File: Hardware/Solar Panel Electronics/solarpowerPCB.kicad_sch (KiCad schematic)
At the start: 45 parts, among them J3 Conn_01x02_Male, J4 Conn_01x06_Male, J5 Conn_01x02_Male, Q1 MMDT2222A, U1 SN65HVD230, U2 ESP32-PICO-D4

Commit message: Started pcb layout
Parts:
- gave numbers to parts that had none: 4
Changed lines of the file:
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@@
   (symbol (lib_id "Device:L") (at 137.16 26.67 90) (unit 1)
     (in_bom yes) (on_board yes)
-    (property "Reference" "L?" (id 0) (at 137.16 21.844 90))
+    (property "Reference" "L3" (id 0) (at 137.16 21.844 90))
     (property "Value" "LQG15WZ1N8B02D" (id 1) (at 137.16 24.1554 90))
     (property "Footprint" "Inductor_SMD:L_0603_1608Metric_Pad1.05x0.95mm_HandSolder" (id 2) (at 137.16 26.67 0)
@@
   (symbol (lib_id "Device:C_Small") (at 140.97 31.75 0) (unit 1)
     (in_bom yes) (on_board yes)
-    (property "Reference" "C?" (id 0) (at 143.3068 30.5816 0)
+    (property "Reference" "C39" (id 0) (at 143.3068 30.5816 0)
       (effects (font (size 1.27 1.27)) (justify left))
     )
@@
   (symbol (lib_id "Device:C_Small") (at 133.35 31.75 0) (unit 1)
     (in_bom yes) (on_board yes)
-    (property "Reference" "C?" (id 0) (at 128.27 30.48 0)
+    (property "Reference" "C38" (id 0) (at 128.27 30.48 0)
       (effects (font (size 1.27 1.27)) (justify left))
     )
@@
   (symbol (lib_id "iclr:AMCA31-2R450G-S1F-T3") (at 146.05 26.67 270) (unit 1)
     (in_bom yes) (on_board yes)
-    (property "Reference" "ANT?" (id 0) (at 154.7876 25.3746 90)
+    (property "Reference" "ANT1" (id 0) (at 154.7876 25.3746 90)
       (effects (font (size 1.27 1.27)) (justify left))
     )
@@
   (symbol (lib_id "power:GND") (at 133.35 34.29 0) (unit 1)
     (in_bom yes) (on_board yes)
-    (property "Reference" "#PWR?" (id 0) (at 133.35 40.64 0)
+    (property "Reference" "#PWR0136" (id 0) (at 133.35 40.64 0)
       (effects (font (size 1.27 1.27)) hide)
     )
@@
   (symbol (lib_id "power:GND") (at 140.97 34.29 0) (unit 1)
     (in_bom yes) (on_board yes)
-    (property "Reference" "#PWR?" (id 0) (at 140.97 40.64 0)
+    (property "Reference" "#PWR0137" (id 0) (at 140.97 40.64 0)
       (effects (font (size 1.27 1.27)) hide)
     )
@@
       (reference "#PWR0135") (unit 1) (value "+3.3V") (footprint "")
     )
+    (path "/673f1a23-6661-4620-90df-f91c1a23f2f1"
+      (reference "#PWR0136") (unit 1) (value "GND") (footprint "")
+    )
+    (path "/d476ee99-f915-47bb-bc5d-98e60df88272"
+      (reference "#PWR0137") (unit 1) (value "GND") (footprint "")
+    )
+    (path "/bc16b27f-da78-4399-84ff-d0e67df4623d/a8cbb7ea-4783-4a46-908f-66157147a7f8"
+      (reference "#PWR0138") (unit 1) (value "GND") (footprint "")
+    )
     (path "/00000000-0000-0000-0000-0000624b2440/00000000-0000-0000-0000-000062471654"
       (reference "#PWR0145") (unit 1) (value "GND") (footprint "")
@@
       (reference "#PWR0150") (unit 1) (value "GND") (footprint "")
     )
-    (path "/673f1a23-6661-4620-90df-f91c1a23f2f1"
-      (reference "#PWR?") (unit 1) (value "GND") (footprint "")
-    )
-    (path "/d476ee99-f915-47bb-bc5d-98e60df88272"
-      (reference "#PWR?") (unit 1) (value "GND") (footprint "")
-    )
     (path "/661e63a6-57d4-4bd6-8435-e9e47baf2ef9"
-      (reference "ANT?") (unit 1) (value "AMCA31-2R450G-S1F-T3") (footprint "iclr:ANT_AMCA31-2R450G-S1F-T3")
+      (reference "ANT1") (unit 1) (value "AMCA31-2R450G-S1F-T3") (footprint "iclr:ANT_AMCA31-2R450G-S1F-T3")
     )
     (path "/00000000-0000-0000-0000-0000620b2ec1"
@@
       (reference "C37") (unit 1) (value "10uF") (footprint "Capacitor_SMD:C_0603_1608Metric")
     )
+    (path "/58323f1b-ca2a-4c1d-b699-a594d763332c"
+      (reference "C38") (unit 1) (value "33pF") (footprint "Capacitor_SMD:C_0603_1608Metric")
+    )
     (path "/43108d1f-6fab-4012-bb34-effc39df9879"
-      (reference "C?") (unit 1) (value "100pF") (footprint "Capacitor_SMD:C_0603_1608Metric")
-    )
-    (path "/58323f1b-ca2a-4c1d-b699-a594d763332c"
-      (reference "C?") (unit 1) (value "33pF") (footprint "Capacitor_SMD:C_0603_1608Metric")
+      (reference "C39") (unit 1) (value "100pF") (footprint "Capacitor_SMD:C_0603_1608Metric")
     )
     (path "/0b74af2e-d916-4a23-ae3b-0ce9a9c64af1"
@@
     )
     (path "/1cf3aab9-4829-448a-a3c1-5a595217a91d/d4a89851-f343-4a84-b3cb-1339eebcb206"
-      (reference "J7") (unit 1) (value "~") (footprint "Connector_Card:microSD_HC_Hirose_DM3AT-SF-PEJM5")
+      (reference "J7") (unit 1) (value "~") (footprint "Connector_Card:microSD_HC_Wuerth_693072010801")
     )
     (path "/00000000-0000-0000-0000-0000624b2440/357ce087-9bb2-449e-8dc8-378603d15219"
@@
       (reference "J13") (unit 1) (value "Battery Connector") (footprint "Connector_JST:JST_ACH_BM02B-ACHSS-GAN-ETF_1x02-1MP_P1.20mm_Vertical")
     )
+    (path "/bc16b27f-da78-4399-84ff-d0e67df4623d/12783491-f223-4d6c-b1a2-c1bcbb00a602"
+      (reference "J14") (unit 1) (value "Screw_Terminal_5VRail") (footprint "TerminalBlock_TE-Connectivity:TerminalBlock_TE_282834-2_1x02_P2.54mm_Horizontal")
+    )
     (path "/b5ffdb69-0d10-4e56-a878-ea9fd431e3ac"
       (reference "JP1") (unit 1) (value "SolderJumper_2_Open") (footprint "Jumper:SolderJumper-2_P1.3mm_Open_RoundedPad1.0x1.5mm")
@@
     )
     (path "/281cba2a-9a0d-4ba9-ae02-4851a4d5ef54"
-      (reference "L?") (unit 1) (value "LQG15WZ1N8B02D") (footprint "Inductor_SMD:L_0603_1608Metric_Pad1.05x0.95mm_HandSolder")
+      (reference "L3") (unit 1) (value "LQG15WZ1N8B02D") (footprint "Inductor_SMD:L_0603_1608Metric_Pad1.05x0.95mm_HandSolder")
     )
     (path "/b081b074-3171-4535-9bf1-f0e71da78e2a/a79c1d38-64a3-45f9-8914-483eb10099cb"

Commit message: Preliminary Layout done. (46x77mm)
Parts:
- ANT1: value AMCA31-2R450G-S1F-T3 -> (none); footprint iclr:ANT_AMCA31-2R450G-S1F-T3 -> (none)
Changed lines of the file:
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@@
       (effects (font (size 1.27 1.27)) (justify left))
     )
-    (property "Value" "AMCA31-2R450G-S1F-T3" (id 1) (at 154.7876 27.686 90)
+    (property "Value" "" (id 1) (at 154.7876 27.686 90)
       (effects (font (size 1.27 1.27)) (justify left))
     )
-    (property "Footprint" "iclr:ANT_AMCA31-2R450G-S1F-T3" (id 2) (at 146.05 26.67 0)
+    (property "Footprint" "" (id 2) (at 146.05 26.67 0)
       (effects (font (size 1.27 1.27)) (justify left bottom) hide)
     )

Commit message: Layed out parts a bit more
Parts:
- ANT1: value (none) -> AMCA31-2R450G-S1F-T3; footprint (none) -> iclr:ANT_AMCA31-2R450G-S1F-T3
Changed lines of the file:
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@@
       (effects (font (size 1.27 1.27)) (justify left))
     )
-    (property "Value" "" (id 1) (at 154.7876 27.686 90)
+    (property "Value" "AMCA31-2R450G-S1F-T3" (id 1) (at 154.7876 27.686 90)
       (effects (font (size 1.27 1.27)) (justify left))
     )
-    (property "Footprint" "" (id 2) (at 146.05 26.67 0)
+    (property "Footprint" "iclr:ANT_AMCA31-2R450G-S1F-T3" (id 2) (at 146.05 26.67 0)
       (effects (font (size 1.27 1.27)) (justify left bottom) hide)
     )

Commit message: Need to do routing.
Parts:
- removed ANT1: AMCA31-2R450G-S1F-T3, iclr:ANT_AMCA31-2R450G-S1F-T3, symbol iclr:AMCA31-2R450G-S1F-T3
- removed C38: 33pF, Capacitor_SMD:C_0603_1608Metric, symbol Device:C_Small
- removed C39: 100pF, Capacitor_SMD:C_0603_1608Metric, symbol Device:C_Small
- removed L3: LQG15WZ1N8B02D, Inductor_SMD:L_0603_1608Metric_Pad1.05x0.95mm_HandSolder, symbol Device:L
- removed U2: ESP32-PICO-D4, Package_DFN_QFN:QFN-48-1EP_7x7mm_P0.5mm_EP5.3x5.3mm, symbol RF_Module:ESP32-PICO-D4
- added U2: (no value), symbol RF_Module:ESP32-WROOM-32D
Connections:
- net +3V3: now also U2.2 (VDD)
- net BOOT: now also U2.25 (IO0)
- net CAN_RX: now also U2.12 (IO27)
- net CAN_TX: now also U2.11 (IO26)
- net CLKOUT: now also U2.23 (IO15)
- net EN: now also U2.3 (EN)
- net GND: now also U2.1 (GND), U2.15 (GND), U2.38 (GND), U2.39 (GND)
- net HSPI_MISO: now also U2.14 (IO12)
- net HSPI_MOSI: now also U2.16 (IO13)
- net HSPI_SCLK: now also U2.13 (IO14)
- net SCL: now also U2.31 (IO19)
- net SDA: now also U2.30 (IO18)
- net VSPI_MISO: now also U2.28 (IO17)
- net VSPI_MOSI: now also U2.33 (IO21)
- net VSPI_SCLK: now also U2.27 (IO16)
- net ~{ADC_CS}: now also U2.37 (IO23)
- net ~{SD_CS}: now also U2.36 (IO22)
- net at R6.1: now also U2.35 (TXD0/IO1)
- net at R7.1: now also U2.34 (RXD0/IO3)

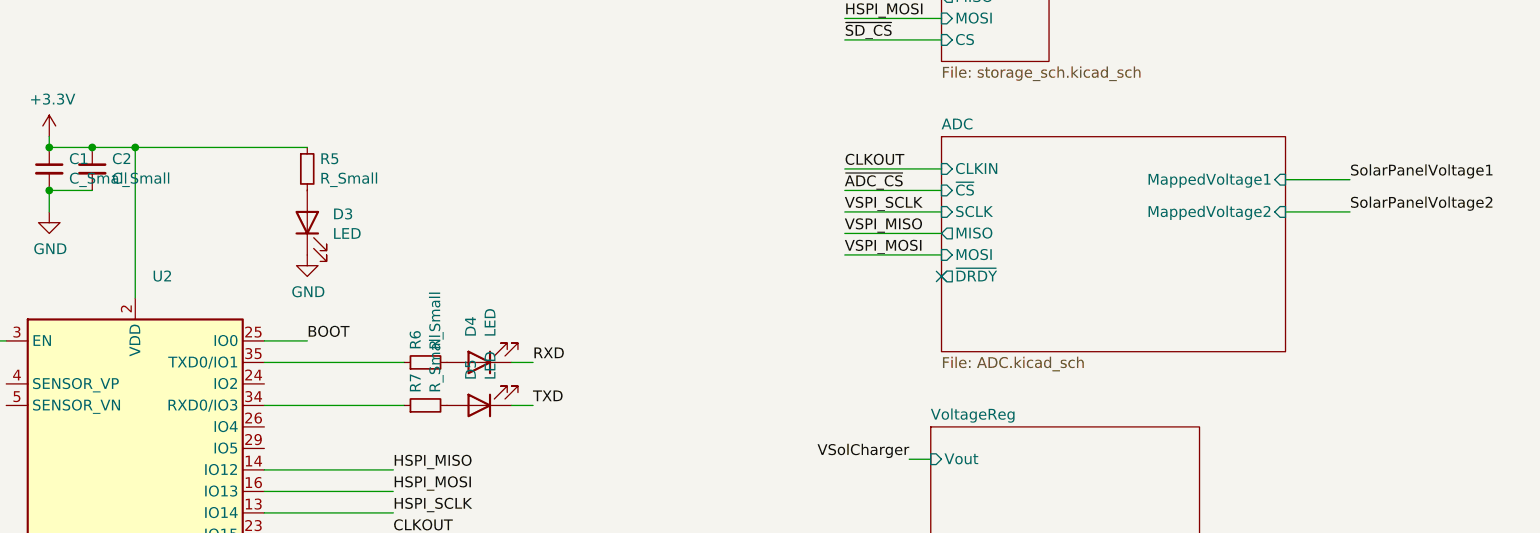
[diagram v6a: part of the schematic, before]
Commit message: Added another ADS component. Layout and routing can be continued.
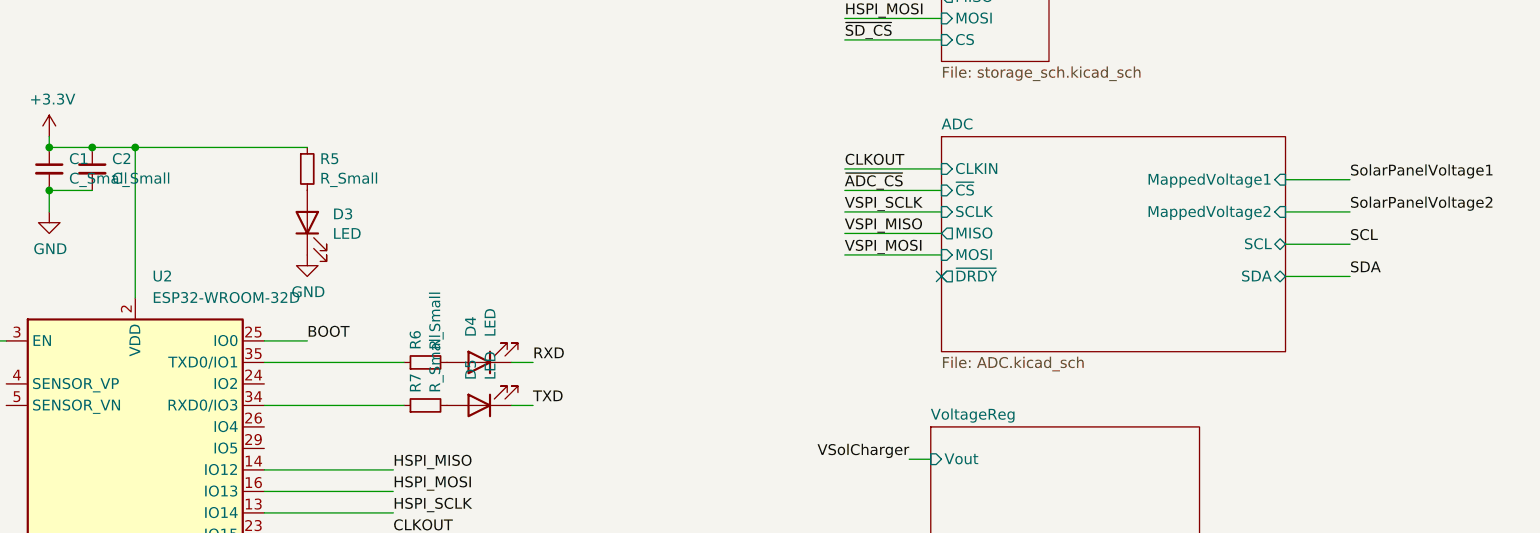
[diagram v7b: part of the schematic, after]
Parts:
- U2: value (none) -> ESP32-WROOM-32D; footprint (none) -> RF_Module:ESP32-WROOM-32
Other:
- sheet ADC ports: added SCL, SDA; removed none
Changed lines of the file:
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@@
+    (stroke (width 0) (type default) (color 0 0 0 0))
+  )
+  (wire (pts (xy 271.78 58.42) (xy 279.4 58.42))
     (stroke (width 0) (type default) (color 0 0 0 0))
   )
@@
     (stroke (width 0) (type default) (color 0 0 0 0))
   )
+  (wire (pts (xy 271.78 54.61) (xy 279.4 54.61))
+    (stroke (width 0) (type default) (color 0 0 0 0))
+  )
   (wire (pts (xy 142.24 176.53) (xy 144.78 176.53))
     (stroke (width 0) (type default) (color 0 0 0 0))
@@
   )
   (label "VSPI_MOSI" (at 166.37 101.6 0)
+    (effects (font (size 1.27 1.27)) (justify left bottom))
+  )
+  (label "SDA" (at 279.4 58.42 0)
     (effects (font (size 1.27 1.27)) (justify left bottom))
   )
@@
   )
   (label "~{ADC_CS}" (at 219.71 48.26 0)
+    (effects (font (size 1.27 1.27)) (justify left bottom))
+  )
+  (label "SCL" (at 279.4 54.61 0)
     (effects (font (size 1.27 1.27)) (justify left bottom))
   )
@@
       (effects (font (size 1.27 1.27)) (justify left))
     )
-    (property "Value" "" (id 1) (at 137.9094 60.96 0)
-      (effects (font (size 1.27 1.27)) (justify left))
-    )
-    (property "Footprint" "" (id 2) (at 135.89 134.62 0)
+    (property "Value" "ESP32-WROOM-32D" (id 1) (at 137.9094 60.96 0)
+      (effects (font (size 1.27 1.27)) (justify left))
+    )
+    (property "Footprint" "RF_Module:ESP32-WROOM-32" (id 2) (at 135.89 134.62 0)
       (effects (font (size 1.27 1.27)) hide)
     )
@@
       (effects (font (size 1.27 1.27)) (justify right))
     )
+    (pin "SCL" bidirectional (at 271.78 54.61 0)
+      (effects (font (size 1.27 1.27)) (justify right))
+    )
+    (pin "SDA" bidirectional (at 271.78 58.42 0)
+      (effects (font (size 1.27 1.27)) (justify right))
+    )
   )
   (sheet (at 229.87 76.2) (size 31.75 16.51) (fields_autoplaced)
@@
       (reference "#PWR033") (unit 1) (value "~") (footprint "")
     )
+    (path "/b081b074-3171-4535-9bf1-f0e71da78e2a/3df830de-4ed6-4e8e-8ec1-513ec29e3820"
+      (reference "#PWR034") (unit 1) (value "+3V3") (footprint "")
+    )
+    (path "/b081b074-3171-4535-9bf1-f0e71da78e2a/24e68f83-3d8e-47b5-a3df-b31b10232af3"
+      (reference "#PWR035") (unit 1) (value "+3V3") (footprint "")
+    )
+    (path "/b081b074-3171-4535-9bf1-f0e71da78e2a/484dc59d-f6ad-45be-b90b-db063f8c0458"
+      (reference "#PWR036") (unit 1) (value "GND") (footprint "")
+    )
+    (path "/b081b074-3171-4535-9bf1-f0e71da78e2a/563f5cf4-541a-47de-98a0-73e57e2bd883"
+      (reference "#PWR037") (unit 1) (value "GND") (footprint "")
+    )
+    (path "/b081b074-3171-4535-9bf1-f0e71da78e2a/4f08d0e8-2b11-4f3b-a2cc-decac7368cd0"
+      (reference "#PWR038") (unit 1) (value "+3V3") (footprint "")
+    )
+    (path "/b081b074-3171-4535-9bf1-f0e71da78e2a/59c30245-2cf8-4c8b-8c9b-82b421fee277"
+      (reference "#PWR039") (unit 1) (value "+3V3") (footprint "")
+    )
+    (path "/b081b074-3171-4535-9bf1-f0e71da78e2a/b15eb05f-55cd-4418-ae5c-34ca4693c1b9"
+      (reference "#PWR040") (unit 1) (value "~") (footprint "")
+    )
+    (path "/b081b074-3171-4535-9bf1-f0e71da78e2a/e110550d-d8af-4452-94b9-caa98717e1e0"
+      (reference "#PWR041") (unit 1) (value "~") (footprint "")
+    )
+    (path "/b081b074-3171-4535-9bf1-f0e71da78e2a/7d3b4ac2-8edd-4e60-96bc-1bd81d41ef7c"
+      (reference "#PWR042") (unit 1) (value "+3.3V") (footprint "")
+    )
     (path "/310f8558-c797-476e-8a2a-d62ef2751219"
       (reference "#PWR0101") (unit 1) (value "GND") (footprint "")
@@
       (reference "C37") (unit 1) (value "10uF") (footprint "Capacitor_SMD:C_0603_1608Metric")
     )
+    (path "/b081b074-3171-4535-9bf1-f0e71da78e2a/7a780f35-04b0-4a70-81b2-6d9de07f75bb"
+      (reference "C38") (unit 1) (value "0.1uF") (footprint "Capacitor_SMD:C_0603_1608Metric")
+    )
+    (path "/b081b074-3171-4535-9bf1-f0e71da78e2a/d4726cc0-5e09-4a99-a798-cb63d71ad832"
+      (reference "C39") (unit 1) (value "10uF") (footprint "Capacitor_SMD:C_0603_1608Metric")
+    )
     (path "/bc16b27f-da78-4399-84ff-d0e67df4623d/9dca0f2d-fbf5-429a-9c58-13009d517f37"
       (reference "C40") (unit 1) (value "2.2u") (footprint "Capacitor_SMD:C_0603_1608Metric")
@@
       (reference "R47") (unit 1) (value "1M") (footprint "Resistor_SMD:R_0603_1608Metric")
     )
+    (path "/b081b074-3171-4535-9bf1-f0e71da78e2a/aca58525-7843-4132-b10b-c43af6da5165"
+      (reference "R48") (unit 1) (value "10k") (footprint "Resistor_SMD:R_0603_1608Metric")
+    )
+    (path "/b081b074-3171-4535-9bf1-f0e71da78e2a/f78c5097-3e5b-47b4-ba35-84f73a0dd4ef"
+      (reference "R49") (unit 1) (value "1k") (footprint "Resistor_SMD:R_0603_1608Metric")
+    )
+    (path "/b081b074-3171-4535-9bf1-f0e71da78e2a/97653713-8f53-424e-9437-3e17f0a974cf"
+      (reference "R50") (unit 1) (value "1k") (footprint "Resistor_SMD:R_0603_1608Metric")
+    )
     (path "/b081b074-3171-4535-9bf1-f0e71da78e2a/2aa0d205-a9fc-441e-ac32-25aab2685fc5"
       (reference "R_Shunt1") (unit 1) (value "1k") (footprint "Resistor_SMD:R_0603_1608Metric")
@@
       (reference "U8") (unit 1) (value "ADS131M04") (footprint "Package_DFN_QFN:WQFN-20-1EP_3x3mm_P0.4mm_EP1.7x1.7mm_ThermalVias")
     )
-  )
+    (path "/b081b074-3171-4535-9bf1-f0e71da78e2a/edc90cf2-db35-4c18-ae81-6ad3becf21d1"
+      (reference "U9") (unit 1) (value "ADS1219IPWT") (footprint "ADS1219IPWT:SOP65P640X120-16N")
+    )
+  )

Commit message: ICARUS v2
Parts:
- removed TP1, TP2: TestPoint, TestPoint:TestPoint_Pad_D1.0mm, symbol Connector:TestPoint
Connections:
- net CLKOUT: no longer names the net of U2.23 (IO15)
- net VSPI_MISO: no longer names the net of U2.28 (IO17)
- net VSPI_MOSI: no longer names the net of U2.33 (IO21)
- net VSPI_SCLK: no longer names the net of U2.27 (IO16)
- net ~{ADC_CS}: no longer names the net of U2.37 (IO23)
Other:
- sheet ADC ports: added none; removed CLKIN, MISO, MOSI, SCLK, ~{CS}
